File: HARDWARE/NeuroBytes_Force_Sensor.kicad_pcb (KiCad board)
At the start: 2 copper layers, 54 x 19 mm, 25 parts, among them P1 JST_GH_5-pos, P6 CONN_01X04, P7 CONN_01X04, Q1 MMBT3904, Q2 MMBT3904, Q3 MMBT3904, SW1 SW_PUSH, U1 STM32L011Gx, U2 3v3 LDO

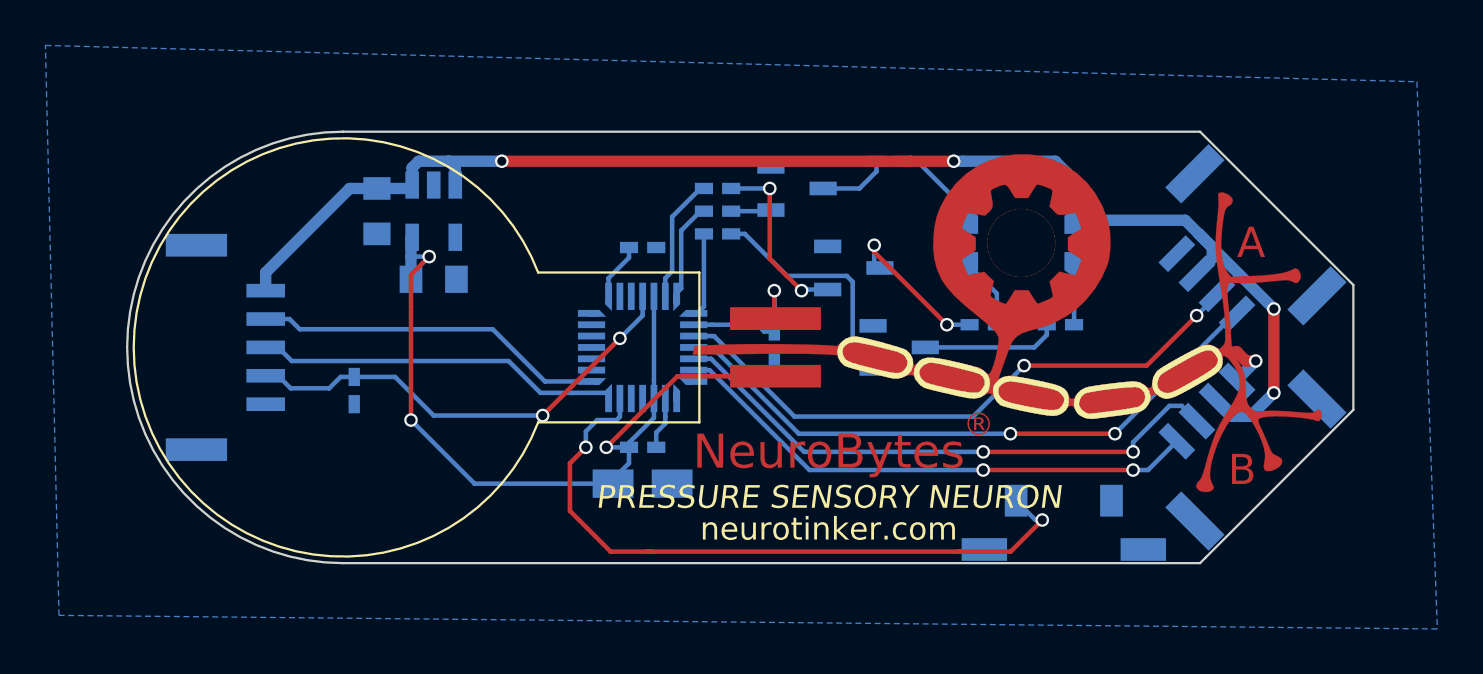
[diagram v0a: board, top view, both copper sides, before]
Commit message: added ESD protection
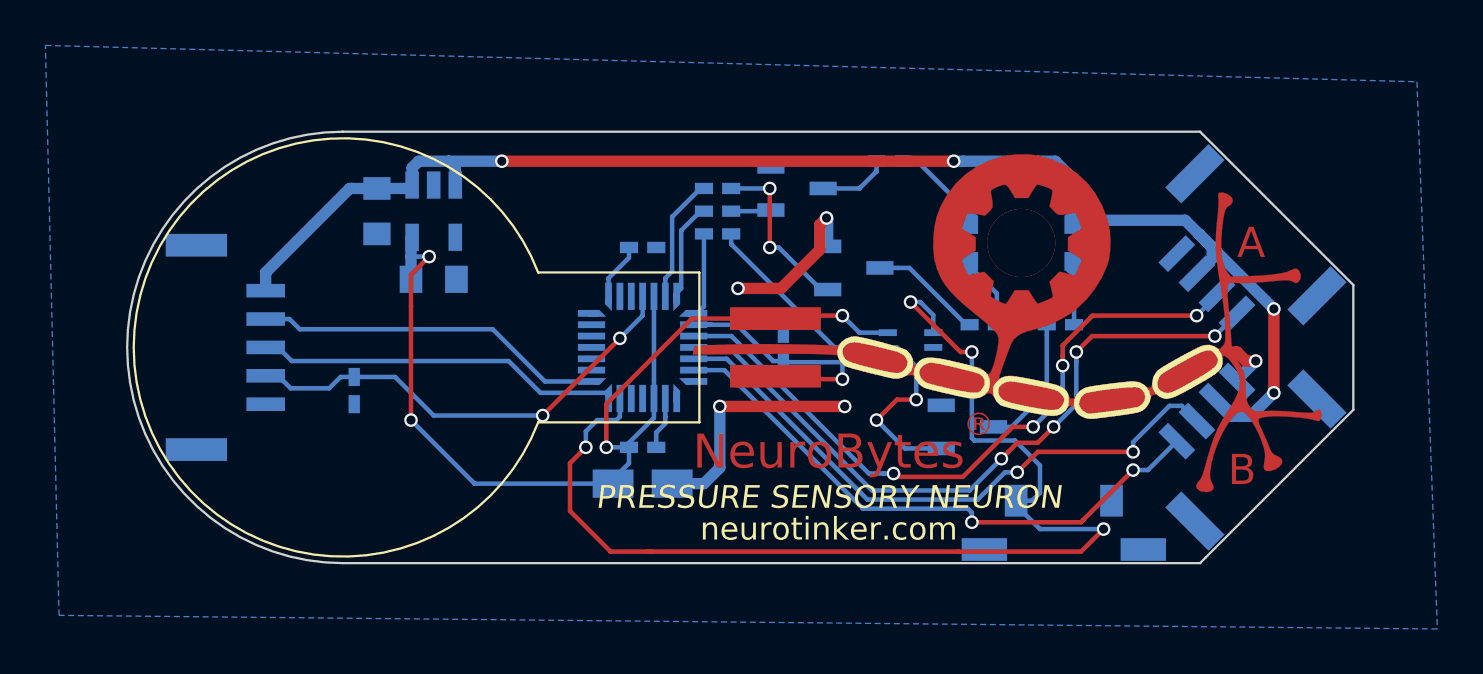
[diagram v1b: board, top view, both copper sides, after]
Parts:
- added U3: RClamp0503F, KiCad_Footprints:ZF_SMD_SOT-353, B.Cu at (125.0, 81.0)
- moved Q3 4.61 mm to (127.5, 84.5)
- moved R8 0.41 mm to (119.4, 81.0), turned to 90 degrees
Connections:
- R9 pad 1: +3V3 -> SENSE
- R9 pad 2: SENSE -> +3V3
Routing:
- net IDENTIFY: track 30.3 -> 51.2 mm, vias 2 -> 4
- net GND: track 4.84 -> 22.5 mm, vias 1 -> 5
- net +3V3: track 38.9 -> 46.4 mm, vias 3 -> 4
- net Net-(Q3-Pad1): track 10.4 -> 17.8 mm, vias 0 -> 2
- net SENSE: track 6.82 -> 13.1 mm
- net A1IN: track 26.8 -> 30.5 mm, vias 2 -> 4
- net A1EX: track 27.7 -> 31.2 mm, vias 2 -> 4
- net A2EX: track 23.6 -> 25.8 mm
- net Net-(Q2-Pad3): track 7.23 -> 5.29 mm, vias 2 -> 0
- net A2IN: track 25.2 -> 27.0 mm
